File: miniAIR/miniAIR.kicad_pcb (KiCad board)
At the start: 2 copper layers, 80 x 50 mm, 18 parts, among them J1 Conn_relay, J2 Conn_HV_IN, J3 Conn_HV_OUT, J4 Conn_pwr, K1 Relay_SPST-NO, Q1 2N7002, U1 LTO150_TB7, U2 LTO150_TB7

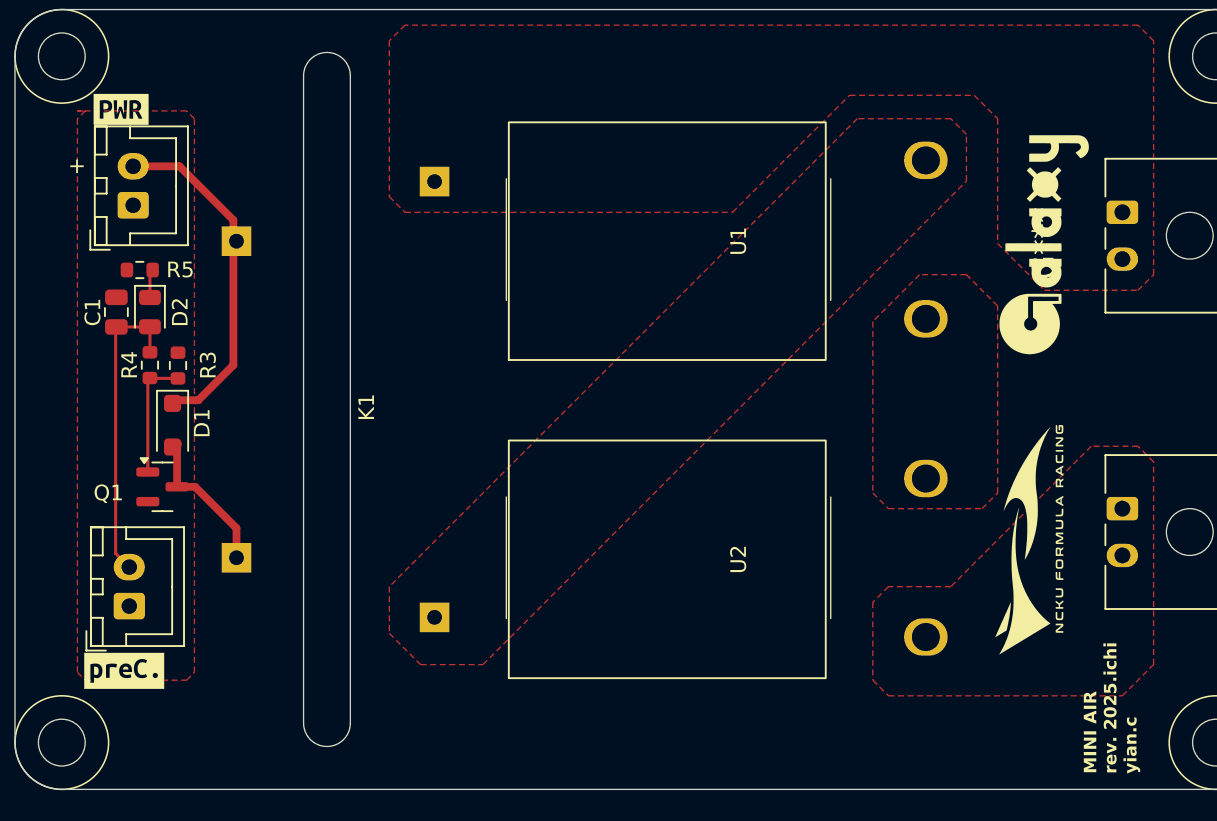
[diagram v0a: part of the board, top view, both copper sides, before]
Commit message: fix: reverse the input logic
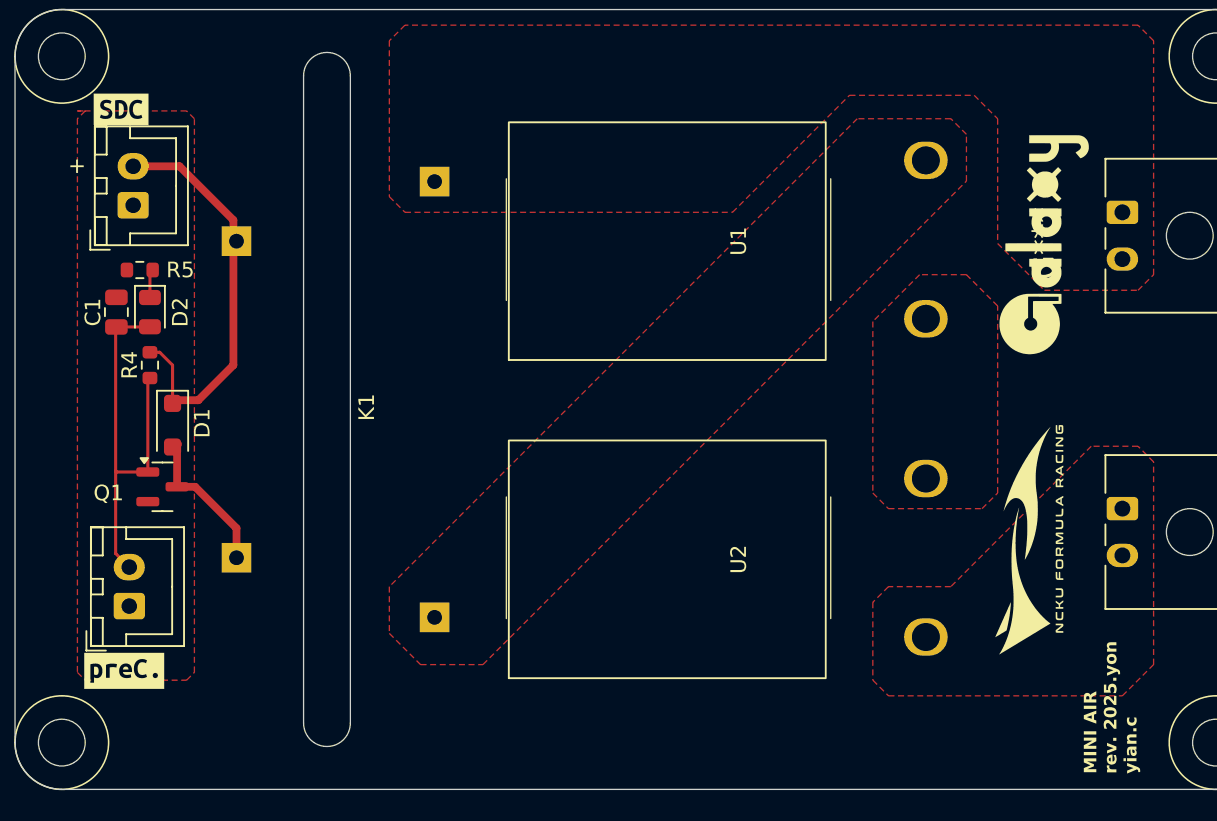
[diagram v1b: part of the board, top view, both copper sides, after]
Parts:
- removed R3: 10k, Resistor_SMD:R_0603_1608Metric
- removed kibuzzard-67D18FC2: G***, kibuzzard-67D18FC2
- added kibuzzard-680B4203: G***, kibuzzard-680B4203, F.Cu at (116.8, 66.4)
- D1: value S1MSWFQ-7 -> 1N4147W
- J4: value Conn_pwr -> Conn_SDC
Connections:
- D1 pad 1: +24V -> VDC
- J4 pad 2: +24V -> VDC
- K1 pad A1: +24V -> VDC
- Q1 pad 1: Net-(Q1-G) -> Net-(D2-A)
- R4 pad 1: Net-(D2-A) -> VDC
- R4 pad 2: Net-(Q1-G) -> Net-(D2-A)
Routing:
- net VDC: track 0.00 -> 25.9 mm
- net +24V: track 21.6 -> 0.00 mm
- net Net-(Q1-G): track 7.89 -> 0.00 mm
- net Net-(D2-A): track 19.6 -> 26.1 mm
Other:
- board text added: "MINI AIR rev. 2025.yon yian.c"
- board text removed: "MINI AIR rev. 2025.ichi yian.c"

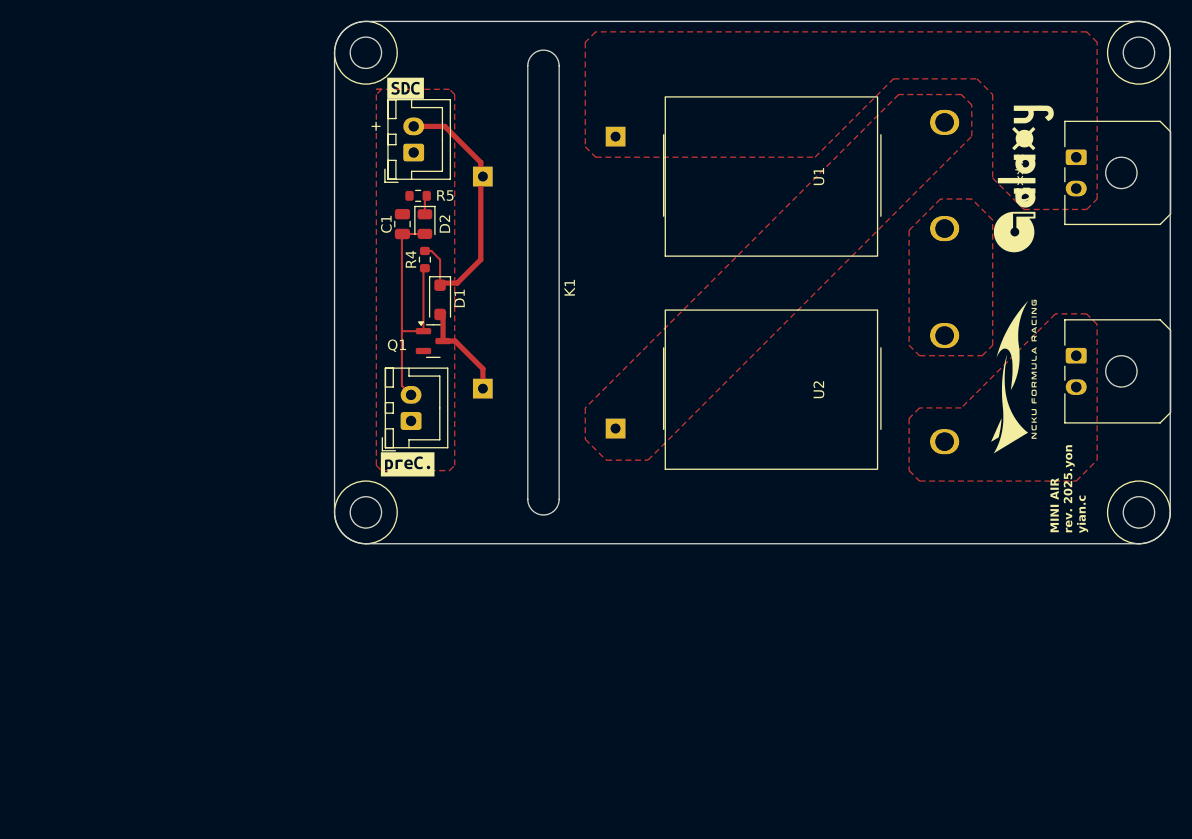
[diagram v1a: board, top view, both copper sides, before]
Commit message: feat: Replace PreC resistor by LPS300
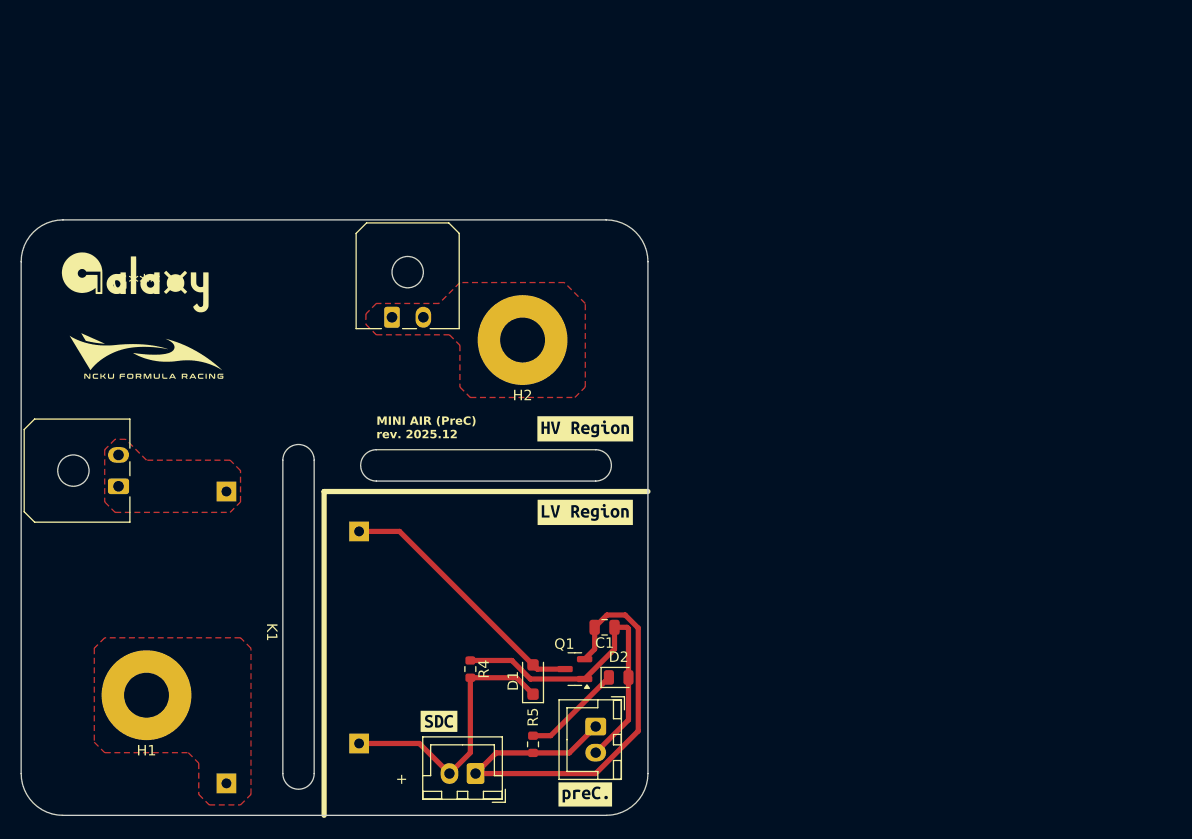
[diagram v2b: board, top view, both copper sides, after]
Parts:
- removed U1, U2: LTO150_TB7, Library:LTO150-TB7
- added H1: LPS300_IN, MountingHole:MountingHole_4.3mm_M4_Pad, F.Cu at (92.0, 124.5)
- added H2: LSP300OUT, MountingHole:MountingHole_4.3mm_M4_Pad, F.Cu at (128.0, 90.5)
- added kibuzzard-69513D27: G***, kibuzzard-69513D27, F.Cu at (134.0, 107.0)
- added kibuzzard-69513D2F: G***, kibuzzard-69513D2F, F.Cu at (134.0, 99.0)
- moved J2 96.9 mm to (89.3, 104.5), turned to 90 degrees
- moved G*** 85.6 mm to (91.0, 85.0), turned to 0 degrees
- moved G*** 83.0 mm to (92.0, 92.0), turned to 0 degrees
- moved J3 65.6 mm to (115.5, 88.3), turned to 0 degrees
- moved kibuzzard-680B4203 60.7 mm to (120.0, 127.0)
- moved J4 59.7 mm to (123.5, 132.0), turned to 180 degrees
- moved R5 53.6 mm to (129.0, 129.2), turned to -90 degrees
- moved D2 47.2 mm to (137.2, 122.8), turned to 0 degrees
- moved K1 44.3 mm to (103.5, 118.5), turned to -90 degrees
- moved C1 43.2 mm to (135.8, 118.0), turned to 180 degrees
- moved R4 39.4 mm to (123.0, 122.0), turned to 90 degrees
- moved D1 37.4 mm to (129.0, 123.0), turned to 90 degrees
- moved kibuzzard-67D18FBA 35.9 mm to (134.0, 134.0)
- moved Q1 34.2 mm to (133.0, 122.0), turned to 180 degrees
- moved J1 34.2 mm to (135.0, 127.5), turned to -90 degrees
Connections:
- K1 pad 13: Net-(K1-Pad13) -> Net-(J2-Pin_1)
- K1 pad 14: Net-(J2-Pin_1) -> Net-(H1-Pad1)
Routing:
- net GND: track 0.00 -> 49.1 mm
- net Net-(D1-A): track 9.56 -> 25.2 mm
- net Net-(D2-K): track 1.64 -> 9.57 mm
- net Net-(D2-A): track 26.1 -> 32.4 mm
- net VDC: track 25.9 -> 26.5 mm
- added copper zone on F.Cu, net Net-(H1-Pad1)
- removed copper zone on F.Cu, net GND
- removed copper zone on F.Cu, net Net-(K1-Pad13)
- removed copper zone on F.Cu, net Net-(U1-Pad1)
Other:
- board size 80 x 50 mm -> 60 x 57 mm
- board text added: "MINI AIR (PreC) rev. 2025.12"
- board text removed: "MINI AIR rev. 2025.yon yian.c"
